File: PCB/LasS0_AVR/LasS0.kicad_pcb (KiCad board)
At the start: 2 copper layers, 29.3 x 82 mm, 47 parts, among them J1 CiKe2PinSock, J10 Conn_01x01, J2 CiKe2PinSock, J3 CiKe2PinSock, J4 CiKe2PinSock, J5 ICSP, J6 Conn_01x01, J7 Conn_01x01, J8 Conn_01x01, J9 Conn_01x01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

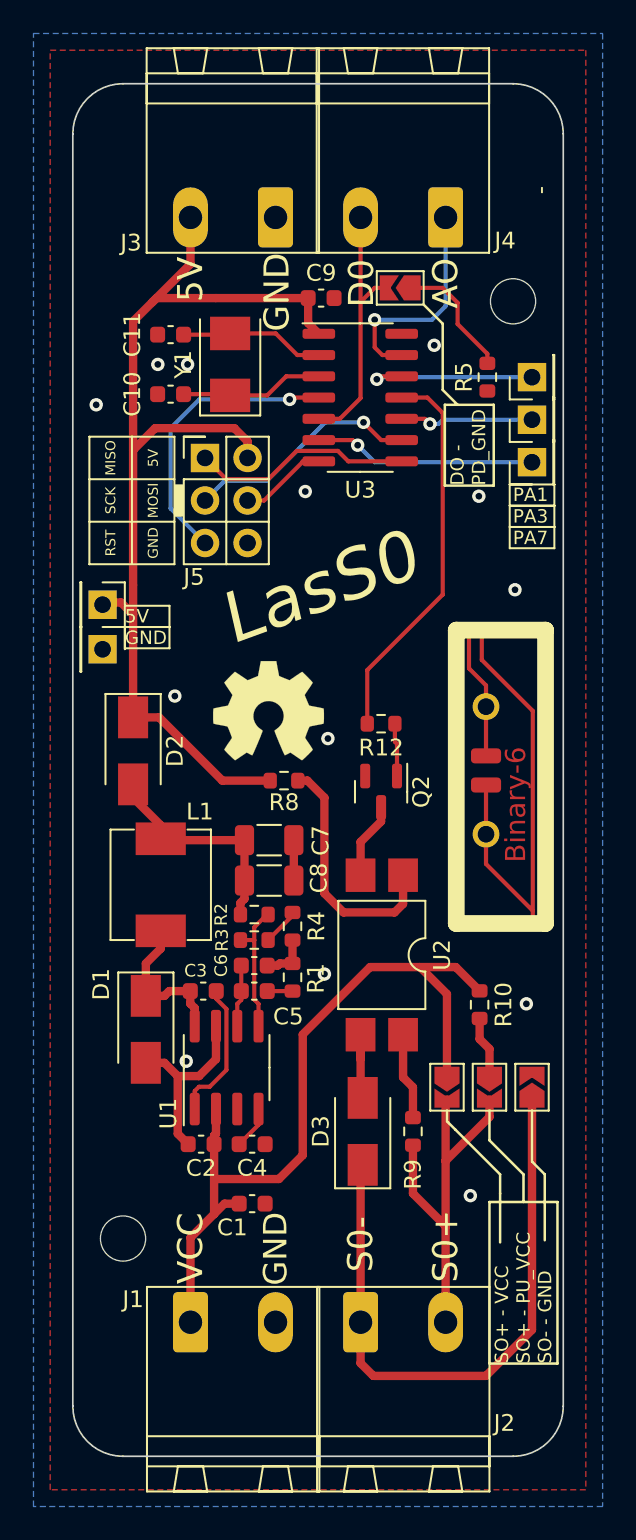
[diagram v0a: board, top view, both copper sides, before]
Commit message: [PCB] Move a via out of silk
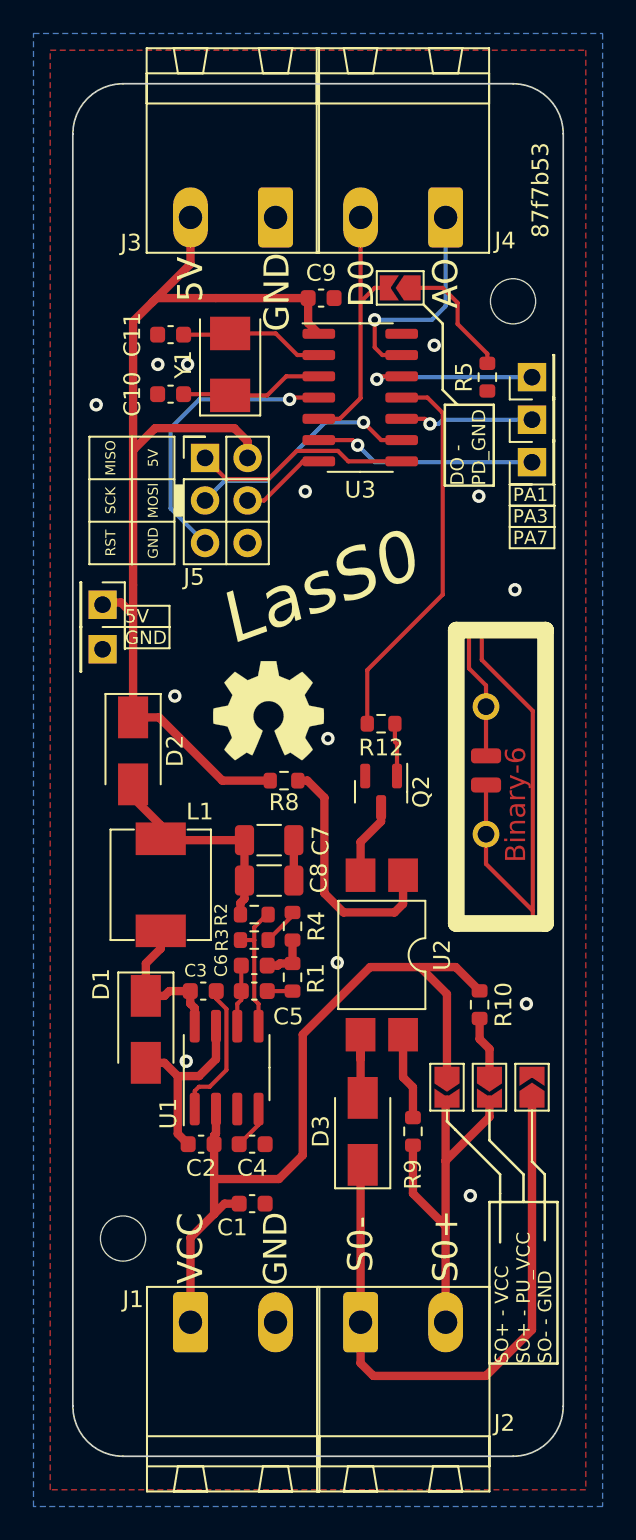
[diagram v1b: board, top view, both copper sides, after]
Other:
- board text added: "87f7b53"
- board text removed: "-"
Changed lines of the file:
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@@
     (effects (font (size 1.5 1.5) (thickness 0.25)))
   )
-  (gr_text "-" (at 161.8 65.356 90) (layer "F.SilkS")
+  (gr_text "87f7b53" (at 161.8 65.356 90) (layer "F.SilkS")
     (effects (font (size 1 1) (thickness 0.15)))
   )
@@
   (via (at 147.748 83.363) (size 0.8) (drill 0.4) (layers "F.Cu" "B.Cu") (free) (net 1))
   (via (at 158.117 83.644) (size 0.8) (drill 0.4) (layers "F.Cu" "B.Cu") (free) (net 1))
-  (via (at 148.891 112.192) (size 0.8) (drill 0.4) (layers "F.Cu" "B.Cu") (free) (net 1))
+  (via (at 149.6588 111.5078) (size 0.8) (drill 0.4) (layers "F.Cu" "B.Cu") (free) (net 1))
   (via (at 139.956 95.582) (size 0.8) (drill 0.4) (layers "F.Cu" "B.Cu") (free) (net 1))
   (via (at 160.276 89.232) (size 0.8) (drill 0.4) (layers "F.Cu" "B.Cu") (free) (net 1))

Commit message: [PCB] Create and order fabrication files
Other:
- board text added: "788734e"
- board text removed: "87f7b53"
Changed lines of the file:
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@@
     (effects (font (size 1.5 1.5) (thickness 0.25)))
   )
-  (gr_text "87f7b53" (at 161.8 65.356 90) (layer "F.SilkS")
+  (gr_text "788734e" (at 161.8 65.356 90) (layer "F.SilkS")
     (effects (font (size 1 1) (thickness 0.15)))
   )

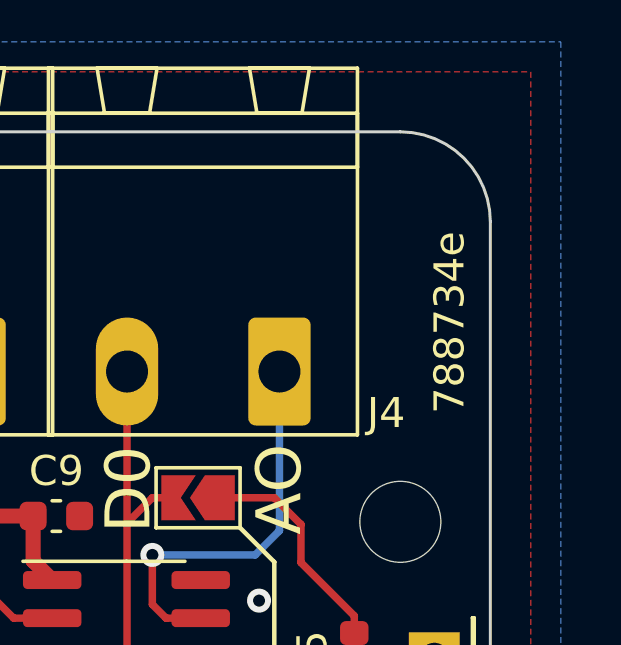
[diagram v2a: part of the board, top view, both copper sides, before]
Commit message: [PCB] update silkscreen documentation, changing GitHub to GitLab
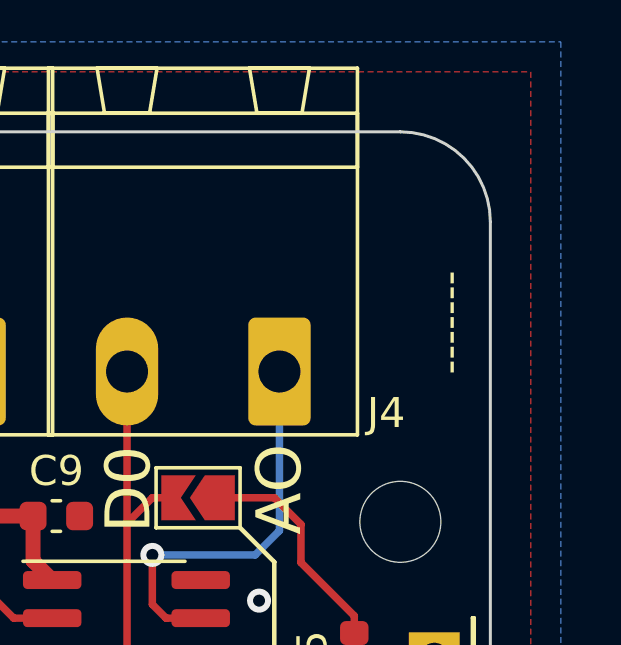
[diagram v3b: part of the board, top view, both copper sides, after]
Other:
- board text added: "-------"
- board text added: "Logic level impulse to S0 converter Chrismettal 2021_07 GitLab.com/Chrismettal/LasS0"
- board text removed: "788734e"
- board text removed: "Logic level impulse to S0 converter Chrismettal 2021_07 github.com/Chrismettal/LasS0"
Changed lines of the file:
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@@
     (effects (font (size 3 3) (thickness 0.75) italic) (justify mirror))
   )
-  (gr_text "Logic level impulse to S0 converter\n\nChrismettal 2021_07\ngithub.com/Chrismettal/LasS0" (at 150.878 100 90) (layer "B.SilkS")
+  (gr_text "Logic level impulse to S0 converter\n\nChrismettal 2021_07\nGitLab.com/Chrismettal/LasS0" (at 150.878 100 90) (layer "B.SilkS")
     (effects (font (size 2 2) (thickness 0.3)) (justify mirror))
   )
@@
     (effects (font (size 1.5 1.5) (thickness 0.25)))
   )
-  (gr_text "788734e" (at 161.8 65.356 90) (layer "F.SilkS")
+  (gr_text "-------" (at 161.8 65.356 90) (layer "F.SilkS")
     (effects (font (size 1 1) (thickness 0.15)))
   )
